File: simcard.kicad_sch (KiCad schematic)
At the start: 10 parts, among them CON4 SIM_CARD

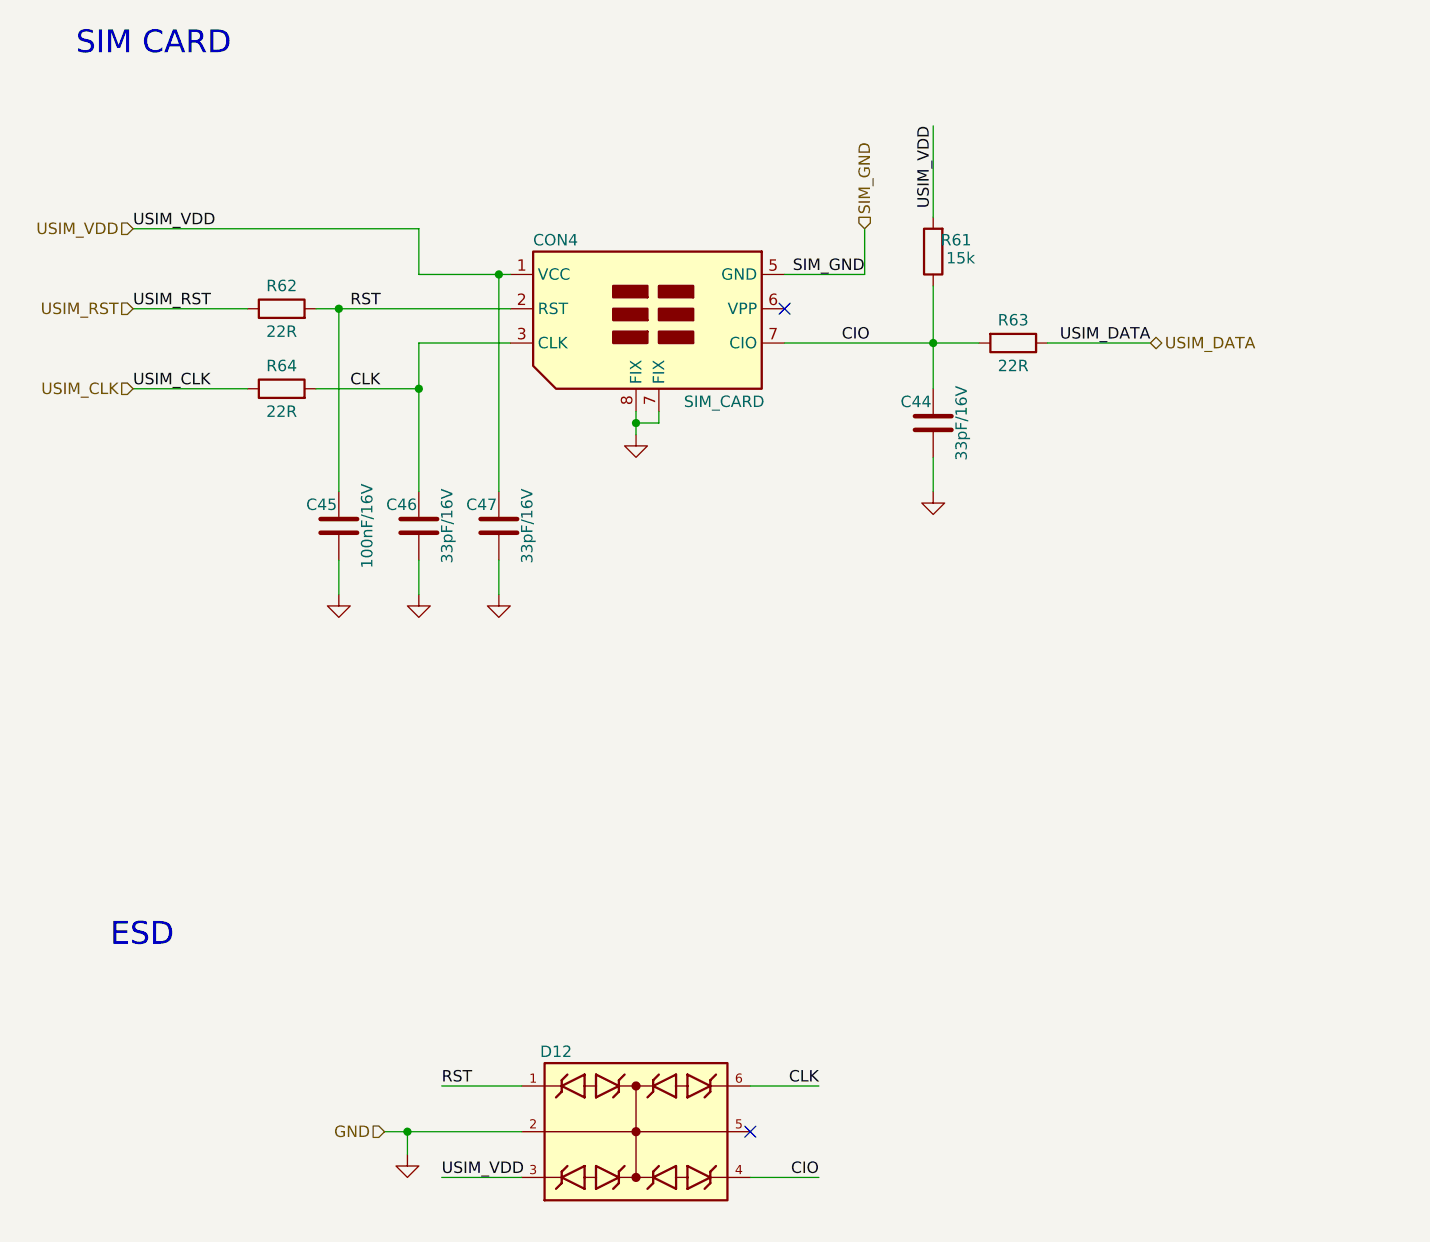
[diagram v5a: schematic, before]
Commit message: Capacitores com encapsulamento 0603
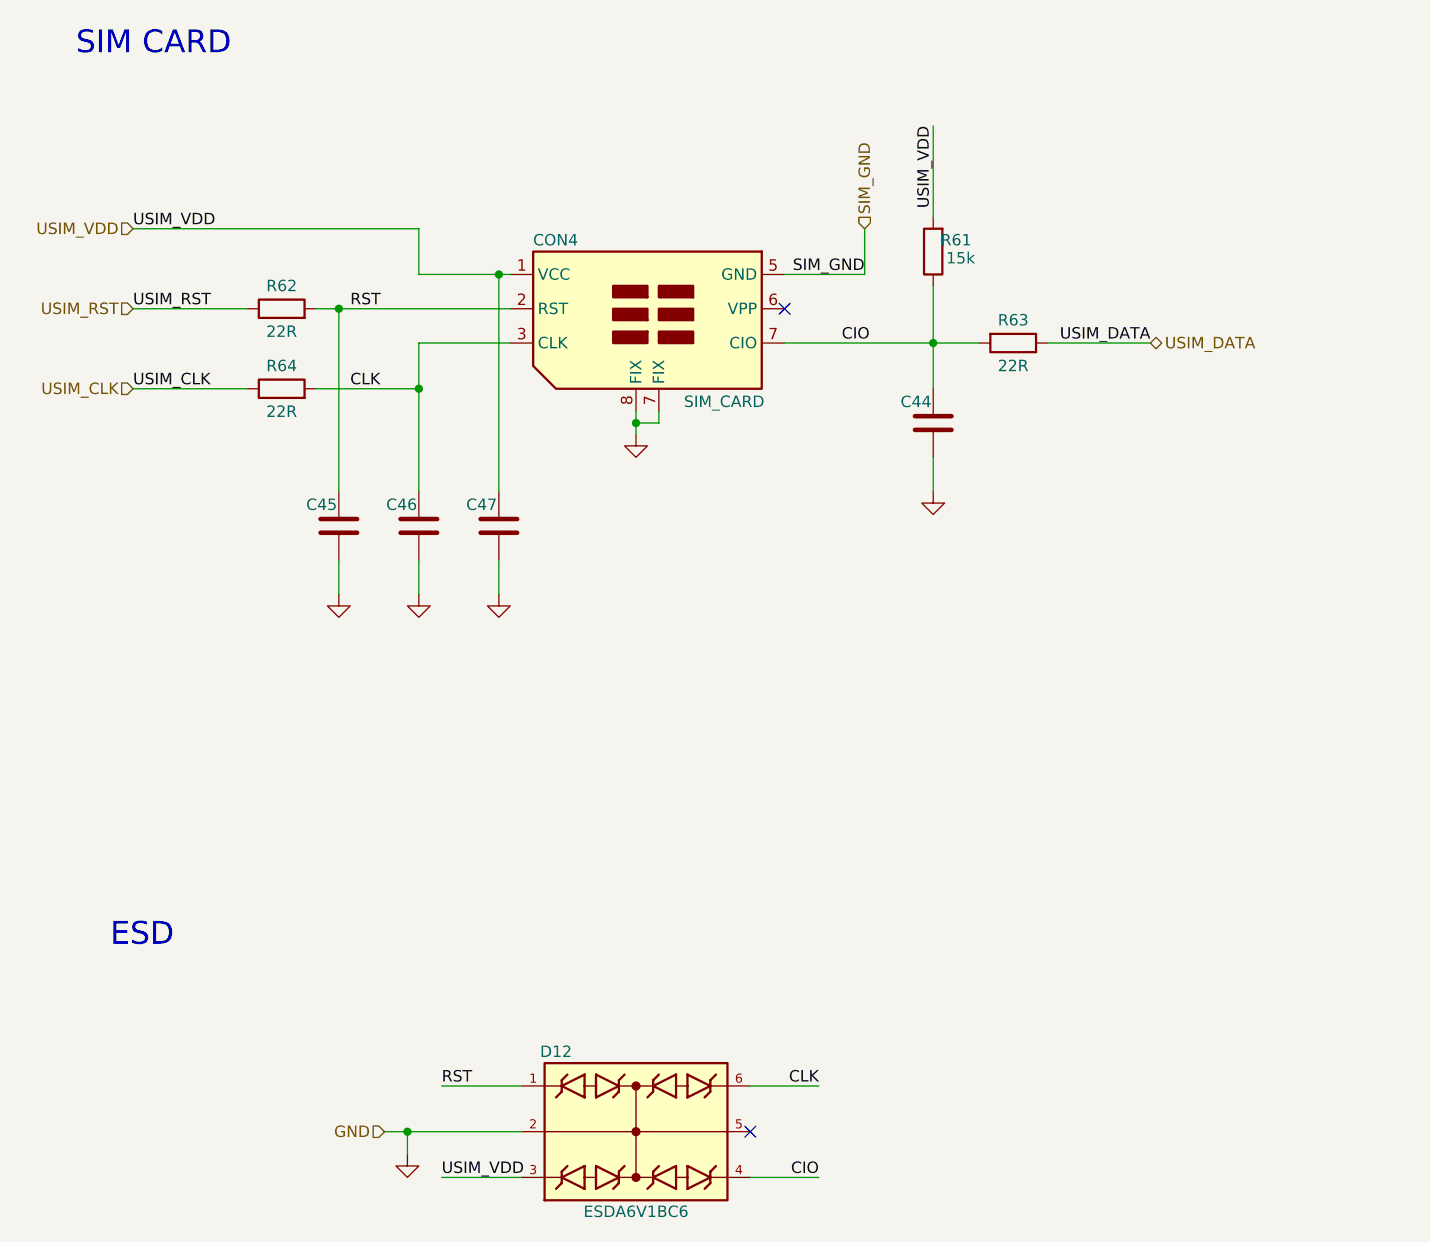
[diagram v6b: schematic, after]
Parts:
- C44, C46, C47: value 33pF/16V -> (none); footprint Capacitor_SMD:C_0402_1005Metric_Pad0.74x0.62mm_HandSolder -> (none)
- C45: value 100nF/16V -> (none); footprint Capacitor_SMD:C_0402_1005Metric_Pad0.74x0.62mm_HandSolder -> (none)
- D12: value (none) -> ESDA6V1BC6; footprint (none) -> Alexandre_Library:ESDA6V1BC6
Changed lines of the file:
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@@
     (in_bom yes) (on_board yes)
     (property "Reference" "C47" (id 0) (at 112.3903 85.2735 0))
-    (property "Value" "33pF/16V" (id 1) (at 117.4454 87.6407 90))
-    (property "Footprint" "Capacitor_SMD:C_0402_1005Metric_Pad0.74x0.62mm_HandSolder" (id 2) (at 115.2652 83.82 0)
+    (property "Value" "" (id 1) (at 117.4454 87.6407 90))
+    (property "Footprint" "" (id 2) (at 115.2652 83.82 0)
       (effects (font (size 1.27 1.27)) hide)
     )
@@
     (in_bom yes) (on_board yes)
     (property "Reference" "C45" (id 0) (at 94.6103 85.2735 0))
-    (property "Value" "100nF/16V" (id 1) (at 99.6654 87.6407 90))
-    (property "Footprint" "Capacitor_SMD:C_0402_1005Metric_Pad0.74x0.62mm_HandSolder" (id 2) (at 97.4852 83.82 0)
+    (property "Value" "" (id 1) (at 99.6654 87.6407 90))
+    (property "Footprint" "" (id 2) (at 97.4852 83.82 0)
       (effects (font (size 1.27 1.27)) hide)
     )
@@
     (in_bom yes) (on_board yes)
     (property "Reference" "D12" (id 0) (at 120.65 146.05 0))
-    (property "Value" "" (id 1) (at 129.54 163.83 0))
-    (property "Footprint" "" (id 2) (at 129.54 143.51 0)
+    (property "Value" "ESDA6V1BC6" (id 1) (at 129.54 163.83 0))
+    (property "Footprint" "Alexandre_Library:ESDA6V1BC6" (id 2) (at 129.54 143.51 0)
       (effects (font (size 1.27 1.27)) (justify left bottom) hide)
     )
@@
     (in_bom yes) (on_board yes)
     (property "Reference" "C44" (id 0) (at 160.6503 73.8435 0))
-    (property "Value" "33pF/16V" (id 1) (at 165.7054 76.2107 90))
-    (property "Footprint" "Capacitor_SMD:C_0402_1005Metric_Pad0.74x0.62mm_HandSolder" (id 2) (at 163.5252 72.39 0)
+    (property "Value" "" (id 1) (at 165.7054 76.2107 90))
+    (property "Footprint" "" (id 2) (at 163.5252 72.39 0)
       (effects (font (size 1.27 1.27)) hide)
     )
@@
     (in_bom yes) (on_board yes)
     (property "Reference" "C46" (id 0) (at 103.5003 85.2735 0))
-    (property "Value" "33pF/16V" (id 1) (at 108.5554 87.6407 90))
-    (property "Footprint" "Capacitor_SMD:C_0402_1005Metric_Pad0.74x0.62mm_HandSolder" (id 2) (at 106.3752 83.82 0)
-      (effects (font (size 1.27 1.27)) hide)
-    )
+    (property "Value" "" (id 1) (at 108.5554 87.6407 90))
+    (property "Footprint" "" (id 2) (at 106.3752 83.82 0)
+      (effects (font (size 1.27 1.27)) hide)
+    )

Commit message: Adicionado os pads dos Test Point e alterado o Bead
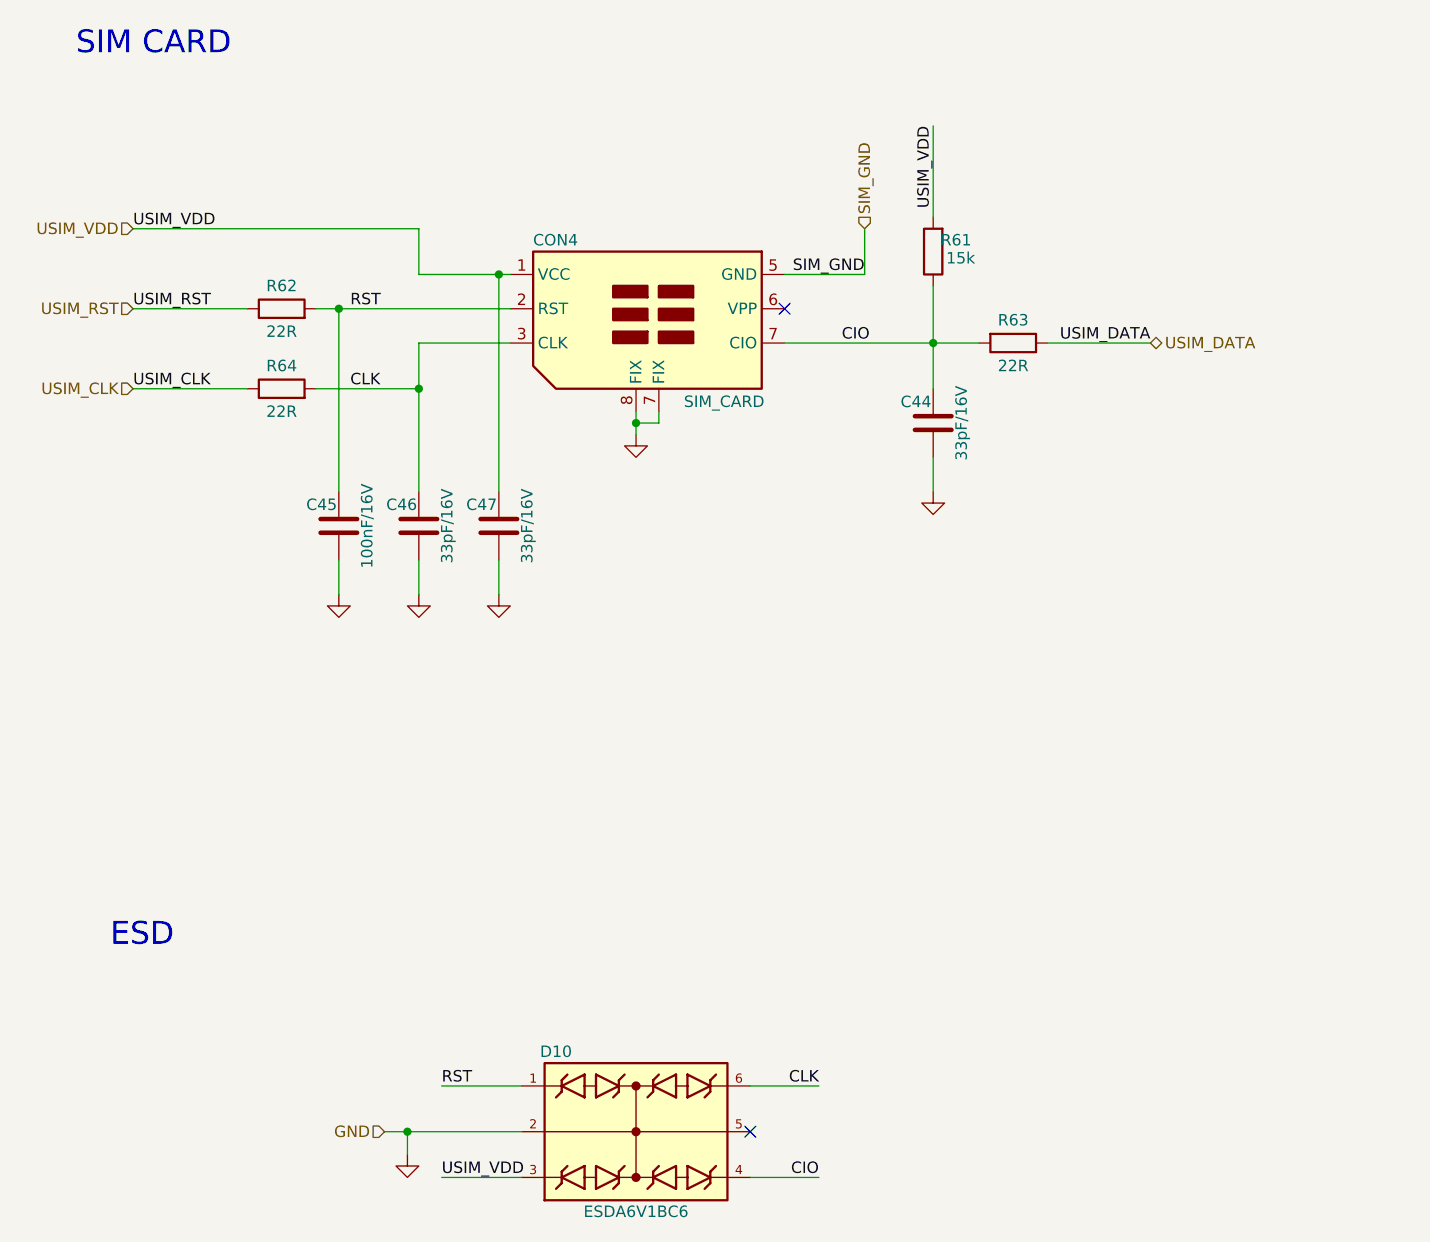
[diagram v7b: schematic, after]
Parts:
- C44, C46, C47: value (none) -> 33pF/16V; footprint (none) -> Capacitor_SMD:C_0603_1608Metric_Pad1.08x0.95mm_HandSolder
- C45: value (none) -> 100nF/16V; footprint (none) -> Capacitor_SMD:C_0603_1608Metric_Pad1.08x0.95mm_HandSolder
- renumbered D12 to D10
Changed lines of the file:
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@@
     (in_bom yes) (on_board yes)
     (property "Reference" "C47" (id 0) (at 112.3903 85.2735 0))
-    (property "Value" "" (id 1) (at 117.4454 87.6407 90))
-    (property "Footprint" "" (id 2) (at 115.2652 83.82 0)
+    (property "Value" "33pF/16V" (id 1) (at 117.4454 87.6407 90))
+    (property "Footprint" "Capacitor_SMD:C_0603_1608Metric_Pad1.08x0.95mm_HandSolder" (id 2) (at 115.2652 83.82 0)
       (effects (font (size 1.27 1.27)) hide)
     )
@@
   (symbol (lib_id "power:GND") (at 162.56 83.82 0) (unit 1)
     (in_bom yes) (on_board yes) (fields_autoplaced)
-    (property "Reference" "#PWR0103" (id 0) (at 162.56 90.17 0)
+    (property "Reference" "#PWR0104" (id 0) (at 162.56 90.17 0)
       (effects (font (size 1.27 1.27)) hide)
     )
@@
   (symbol (lib_id "power:GND") (at 105.41 95.25 0) (unit 1)
     (in_bom yes) (on_board yes) (fields_autoplaced)
-    (property "Reference" "#PWR0105" (id 0) (at 105.41 101.6 0)
+    (property "Reference" "#PWR0106" (id 0) (at 105.41 101.6 0)
       (effects (font (size 1.27 1.27)) hide)
     )
@@
   (symbol (lib_id "power:GND") (at 129.54 77.47 0) (unit 1)
     (in_bom yes) (on_board yes) (fields_autoplaced)
-    (property "Reference" "#PWR0102" (id 0) (at 129.54 83.82 0)
+    (property "Reference" "#PWR0103" (id 0) (at 129.54 83.82 0)
       (effects (font (size 1.27 1.27)) hide)
     )
@@
   (symbol (lib_id "power:GND") (at 96.52 95.25 0) (unit 1)
     (in_bom yes) (on_board yes) (fields_autoplaced)
-    (property "Reference" "#PWR0104" (id 0) (at 96.52 101.6 0)
+    (property "Reference" "#PWR0105" (id 0) (at 96.52 101.6 0)
       (effects (font (size 1.27 1.27)) hide)
     )
@@
   (symbol (lib_id "power:GND") (at 104.14 157.48 0) (unit 1)
     (in_bom yes) (on_board yes) (fields_autoplaced)
-    (property "Reference" "#PWR0136" (id 0) (at 104.14 163.83 0)
+    (property "Reference" "#PWR0108" (id 0) (at 104.14 163.83 0)
       (effects (font (size 1.27 1.27)) hide)
     )
@@
     (in_bom yes) (on_board yes)
     (property "Reference" "C45" (id 0) (at 94.6103 85.2735 0))
-    (property "Value" "" (id 1) (at 99.6654 87.6407 90))
-    (property "Footprint" "" (id 2) (at 97.4852 83.82 0)
+    (property "Value" "100nF/16V" (id 1) (at 99.6654 87.6407 90))
+    (property "Footprint" "Capacitor_SMD:C_0603_1608Metric_Pad1.08x0.95mm_HandSolder" (id 2) (at 97.4852 83.82 0)
       (effects (font (size 1.27 1.27)) hide)
     )
@@
   (symbol (lib_id "Alexandre_Library:ESDA6V1BC6") (at 129.54 154.94 0) (unit 1)
     (in_bom yes) (on_board yes)
-    (property "Reference" "D12" (id 0) (at 120.65 146.05 0))
+    (property "Reference" "D10" (id 0) (at 120.65 146.05 0))
     (property "Value" "ESDA6V1BC6" (id 1) (at 129.54 163.83 0))
     (property "Footprint" "Alexandre_Library:ESDA6V1BC6" (id 2) (at 129.54 143.51 0)
@@
   (symbol (lib_id "power:GND") (at 114.3 95.25 0) (unit 1)
     (in_bom yes) (on_board yes) (fields_autoplaced)
-    (property "Reference" "#PWR0106" (id 0) (at 114.3 101.6 0)
+    (property "Reference" "#PWR0107" (id 0) (at 114.3 101.6 0)
       (effects (font (size 1.27 1.27)) hide)
     )
@@
     (in_bom yes) (on_board yes)
     (property "Reference" "C44" (id 0) (at 160.6503 73.8435 0))
-    (property "Value" "" (id 1) (at 165.7054 76.2107 90))
-    (property "Footprint" "" (id 2) (at 163.5252 72.39 0)
+    (property "Value" "33pF/16V" (id 1) (at 165.7054 76.2107 90))
+    (property "Footprint" "Capacitor_SMD:C_0603_1608Metric_Pad1.08x0.95mm_HandSolder" (id 2) (at 163.5252 72.39 0)
       (effects (font (size 1.27 1.27)) hide)
     )
@@
     (in_bom yes) (on_board yes)
     (property "Reference" "C46" (id 0) (at 103.5003 85.2735 0))
-    (property "Value" "" (id 1) (at 108.5554 87.6407 90))
-    (property "Footprint" "" (id 2) (at 106.3752 83.82 0)
-      (effects (font (size 1.27 1.27)) hide)
-    )
+    (property "Value" "33pF/16V" (id 1) (at 108.5554 87.6407 90))
+    (property "Footprint" "Capacitor_SMD:C_0603_1608Metric_Pad1.08x0.95mm_HandSolder" (id 2) (at 106.3752 83.82 0)
+      (effects (font (size 1.27 1.27)) hide)
+    )
